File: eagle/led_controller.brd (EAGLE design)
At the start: 60 x 55 mm, 12 parts, among them IC1 MC78M05CTG, M1 ARDUINO-NANO-3.0, Q1 TIP120, Q2 TIP120, Q3 TIP120

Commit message: [Eagle] Create new board
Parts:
- moved IQRF 53.7 mm to (4.57, 34.7), turned to 90 degrees
- moved M1 15.8 mm to (37.9, 33.1)
- moved Q1 12.7 mm to (53.1, 54.6)
- moved Q2 10.3 mm to (39.2, 54.6)
- moved Q3 7.91 mm to (25.3, 54.6)
- moved IC1 5.59 mm to (11.3, 58.5)
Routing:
- net N$4: track 68.8 -> 18.5 mm
- net +5V: track 141.4 -> 92.7 mm
- net N$5: track 58.1 -> 18.2 mm
- net N$6: track 52.3 -> 21.2 mm
- net N$7: track 0.00 -> 23.1 mm
- net GND: track 159.6 -> 149.5 mm
- net N$3: track 17.1 -> 25.7 mm
- net N$8: track 32.3 -> 29.0 mm
- net N$9: track 33.7 -> 32.0 mm
- net N$1: track 21.2 -> 19.8 mm
- net N$2: track 6.70 -> 8.06 mm
- net +12V: track 49.1 -> 47.9 mm
- net N$10: track 39.8 -> 38.9 mm
- added copper zone on layer 16, net GND
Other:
- board size 60 x 55 mm -> 60 x 57.5 mm
- board text removed: "Roman Ondráček led_controller 2016 v1.0.0"

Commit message: [Eagle] Update board
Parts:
- moved IQRF 52.6 mm to (57.1, 37.2), turned to 270 degrees
- moved M1 15.2 mm to (22.9, 35.6), turned to 180 degrees
- moved IC1 7.07 mm to (6.35, 63.5)
- moved Q1 5.59 mm to (48.1, 57.1)
- moved Q2 5.59 mm to (34.2, 57.1)
- moved Q3 5.59 mm to (20.3, 57.1)
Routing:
- net GND: track 149.5 -> 50.2 mm
- net N$2: track 8.06 -> 26.5 mm
- net N$1: track 19.8 -> 32.6 mm
- net N$9: track 32.0 -> 41.2 mm
- net +12V: track 47.9 -> 54.3 mm
- net +5V: track 92.7 -> 96.8 mm
- net N$6: track 21.2 -> 25.0 mm
- net N$7: track 23.1 -> 26.5 mm
- net N$10: track 38.9 -> 41.6 mm
- net N$5: track 18.2 -> 20.7 mm
- net N$11: track 5.92 -> 7.01 mm
- net N$3: track 25.7 -> 25.1 mm

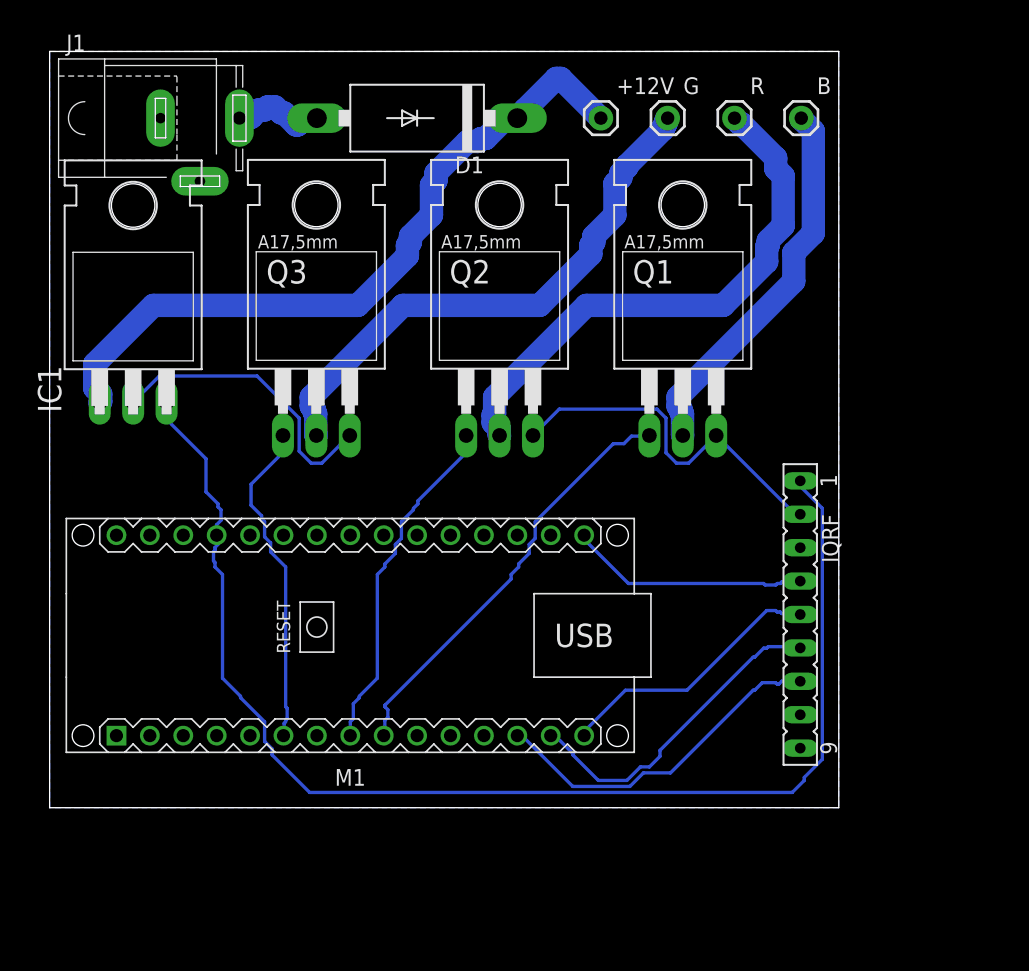
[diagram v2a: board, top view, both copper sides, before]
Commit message: [Eagle] Added schematic and board in pictures
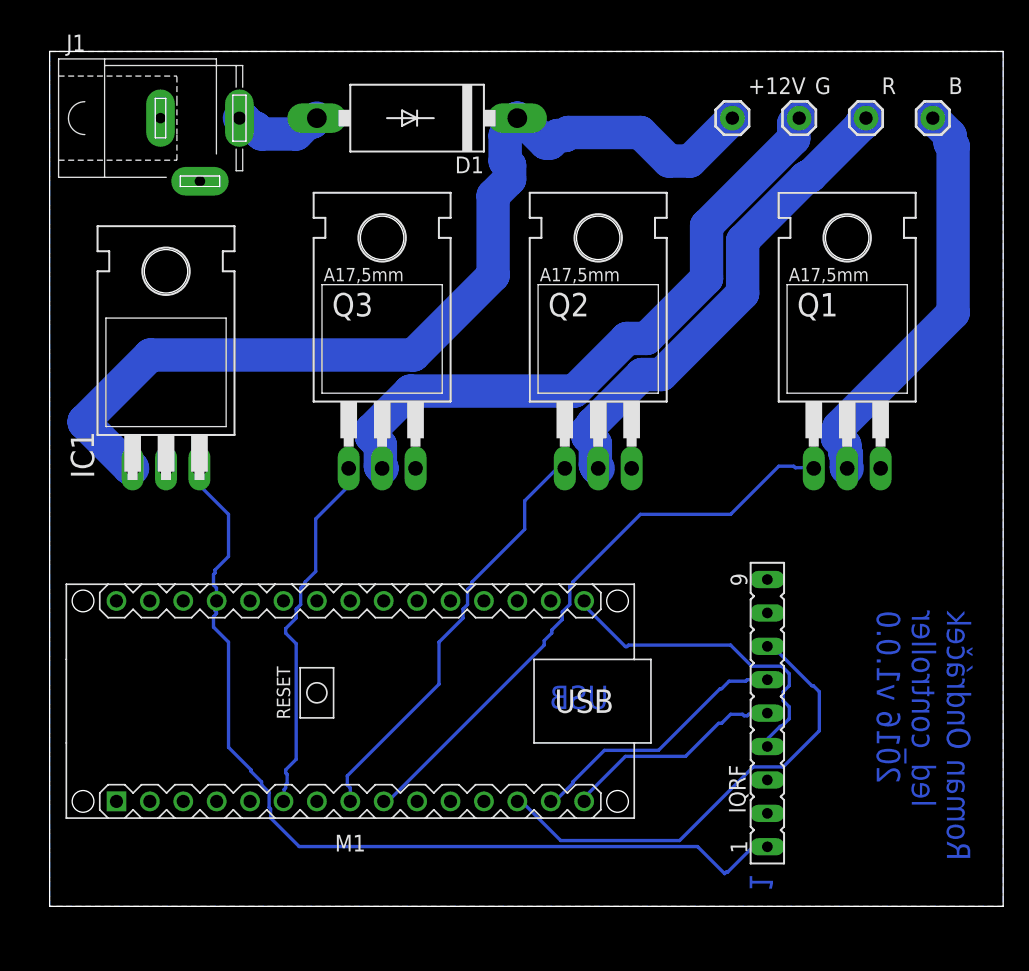
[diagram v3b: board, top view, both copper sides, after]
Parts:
- moved Q1 12.7 mm to (60.6, 54.6)
- moved B 10.0 mm to (67.2, 74.9)
- moved +12V 10.0 mm to (51.9, 74.9)
- moved G 10.0 mm to (57.0, 74.9)
- moved R 10.0 mm to (62.1, 74.9)
- moved Q2 7.91 mm to (41.7, 54.6)
- moved IQRF 7.91 mm to (54.6, 29.7), turned to 90 degrees
- moved IC1 5.59 mm to (8.85, 58.5)
- moved Q3 5.59 mm to (25.3, 54.6)
- moved M1 5.00 mm to (22.9, 30.6)
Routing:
- net GND: track 50.2 -> 0.00 mm
- net +5V: track 96.8 -> 70.4 mm
- net +12V: track 54.3 -> 73.6 mm
- net N$1: track 32.6 -> 44.9 mm
- net N$7: track 26.5 -> 36.0 mm
- net N$10: track 41.6 -> 48.6 mm
- net N$4: track 18.3 -> 24.9 mm
- net N$2: track 26.5 -> 32.6 mm
- net N$6: track 25.0 -> 20.4 mm
- net N$9: track 41.2 -> 36.7 mm
- net N$5: track 20.7 -> 17.0 mm
- net N$3: track 25.1 -> 28.1 mm
- net N$8: track 28.9 -> 31.2 mm
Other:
- board size 60 x 57.5 mm -> 72.5 x 65 mm
- board text added: "1"
- board text added: "Roman Ondráček led_controller 2016 v1.0.0"
- board text added: "USB"
